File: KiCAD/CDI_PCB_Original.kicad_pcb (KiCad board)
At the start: 2 copper layers, 86.9 x 77.7 mm, 45 parts, among them P1 Blue, P10 Green w/ White, P11 Pink, P2 Black w/ White, P3 Yellow, P4 Green Coil, P5 Green Harness, P6 White, P7 Orange, P8 Brown, P9 Light Blue

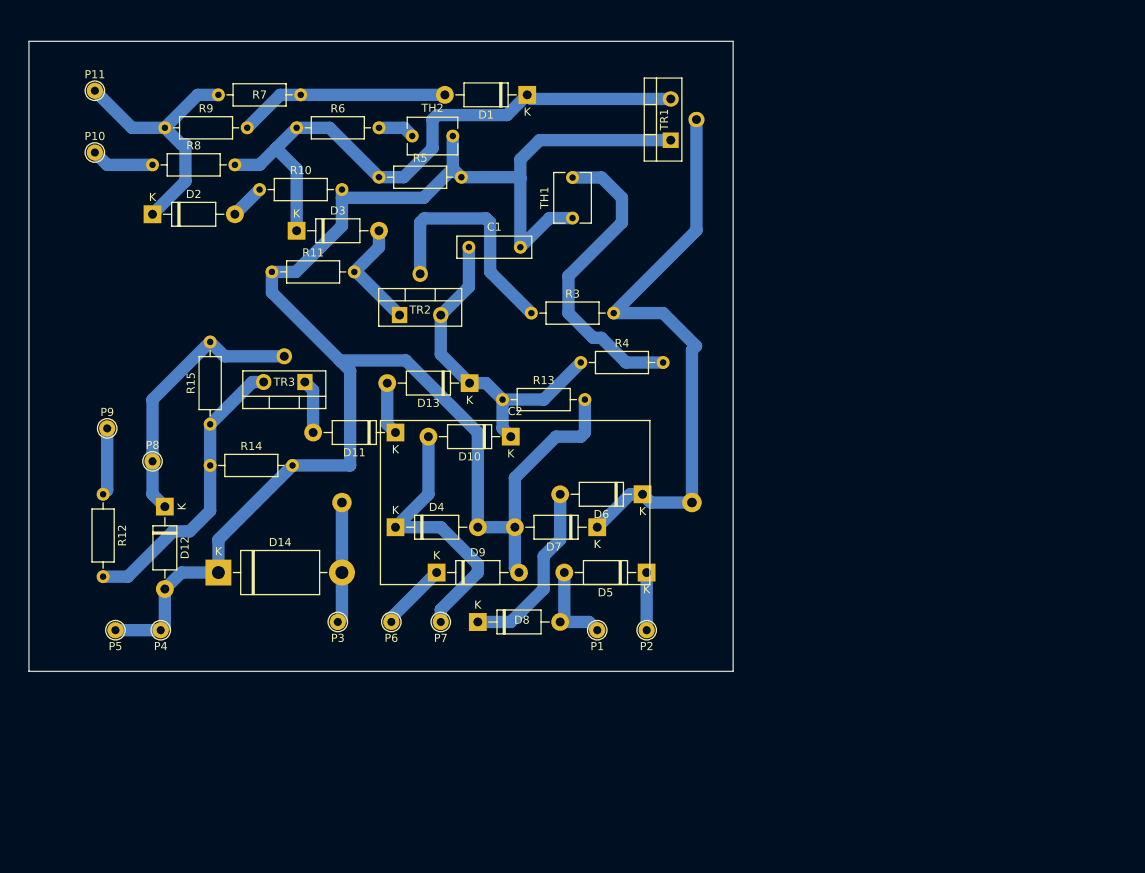
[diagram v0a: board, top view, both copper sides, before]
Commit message: Shrink board down to 3x3.  Flip it so it works with Gerber files so it can be sent off. Back up original design, just in case.  (To be removed in the future)
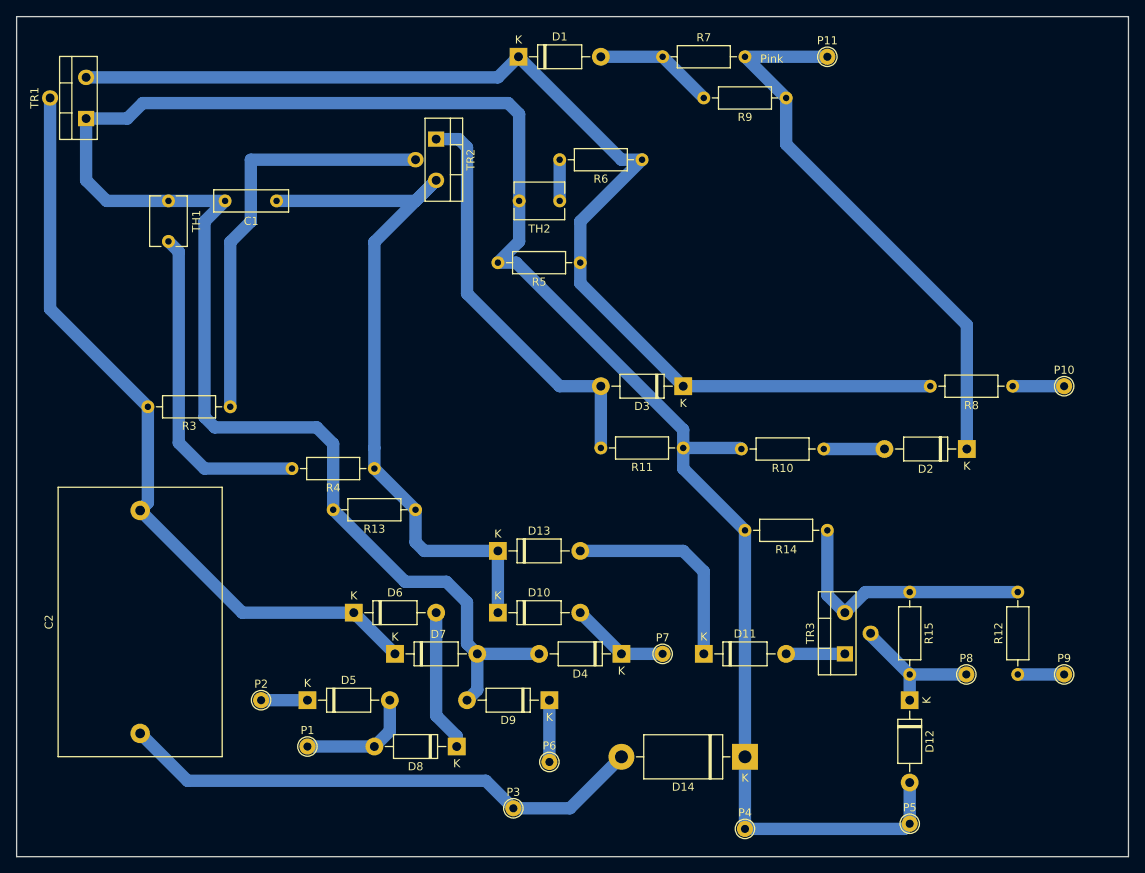
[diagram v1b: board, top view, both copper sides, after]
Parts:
- moved P10 123.0 mm to (228.3, 83.7)
- moved P9 121.9 mm to (228.3, 119.3)
- moved R12 115.0 mm to (222.6, 119.3), turned to 90 degrees
- moved R8 109.6 mm to (221.9, 83.7), turned to 180 degrees
- moved D2 104.5 mm to (216.3, 91.4), turned to 180 degrees
- moved P8 103.8 mm to (216.2, 119.3)
- moved P5 100.8 mm to (209.2, 137.7), turned to 0 degrees
- moved D12 94.9 mm to (209.2, 122.4)
- moved P11 90.5 mm to (199.1, 43.1)
- moved R15 88.7 mm to (209.2, 109.1), turned to -90 degrees
- moved R9 76.7 mm to (194.0, 48.1), turned to 180 degrees
- moved R10 76.6 mm to (198.6, 91.4), turned to 180 degrees
- moved R14 76.6 mm to (199.1, 101.5), turned to 180 degrees
- moved P4 76.1 mm to (188.9, 138.3), turned to 0 degrees
- moved TR3 74.6 mm to (201.2, 116.7), turned to 90 degrees
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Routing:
- net Net-(C1-Pad2): track 216.0 -> 311.1 mm
- net Net-(D1-Pad1): track 75.9 -> 141.7 mm
- net Net-(C2-Pad1): track 14.9 -> 65.8 mm
- net Net-(C1-Pad1): track 41.1 -> 88.9 mm
- net Net-(D2-Pad1): track 32.5 -> 69.9 mm
- net Net-(D3-Pad2): track 14.1 -> 51.1 mm
- net Net-(R3-Pad1): track 28.7 -> 51.9 mm
- net Net-(C2-Pad2): track 73.3 -> 95.0 mm
- net Net-(D10-Pad2): track 33.9 -> 12.3 mm
- net Net-(D11-Pad1): track 6.52 -> 26.5 mm
- net Net-(D12-Pad1): track 33.8 -> 17.2 mm
- net Net-(D1-Pad2): track 26.1 -> 14.8 mm
- net Net-(D6-Pad2): track 22.3 -> 17.6 mm
- net Net-(D5-Pad2): track 11.3 -> 14.8 mm
- net Net-(D2-Pad2): track 4.31 -> 7.49 mm
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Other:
- board size 86.9 x 77.7 mm -> 137.2 x 103.6 mm
- board text added: "Pink"
